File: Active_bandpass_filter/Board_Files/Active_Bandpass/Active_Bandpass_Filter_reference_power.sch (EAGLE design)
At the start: 35 parts, among them IC2 AD8031R, IC3 7805TV, IC5 AD8542R

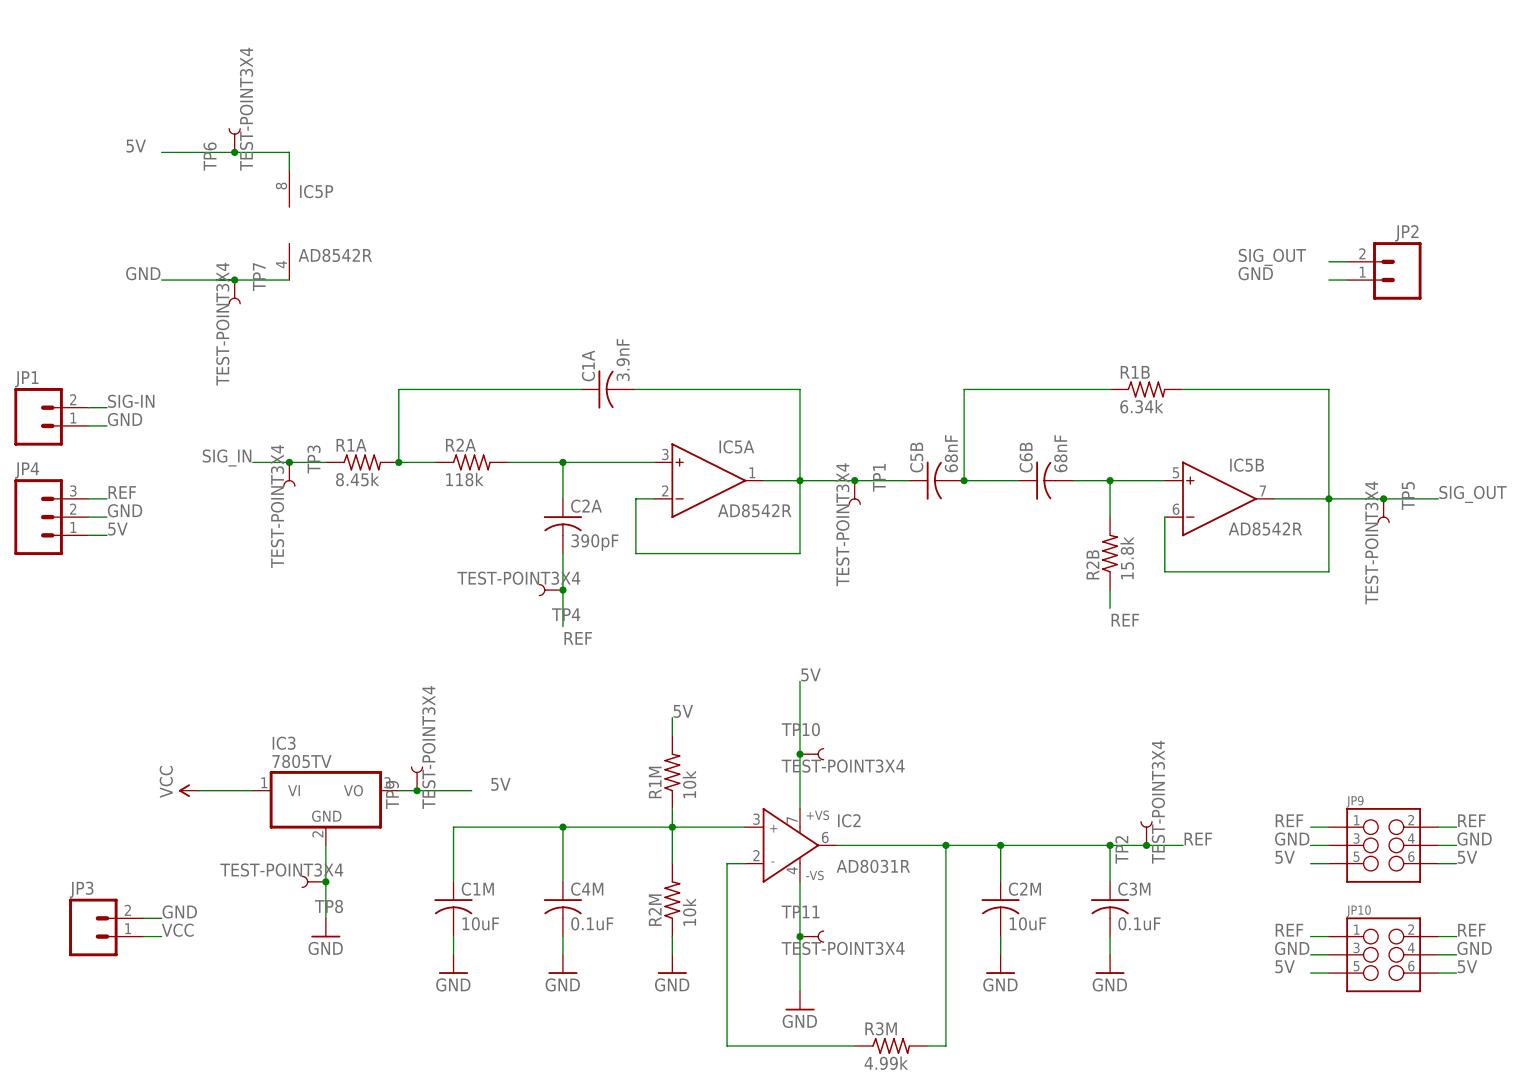
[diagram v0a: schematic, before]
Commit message: split into 2 boards
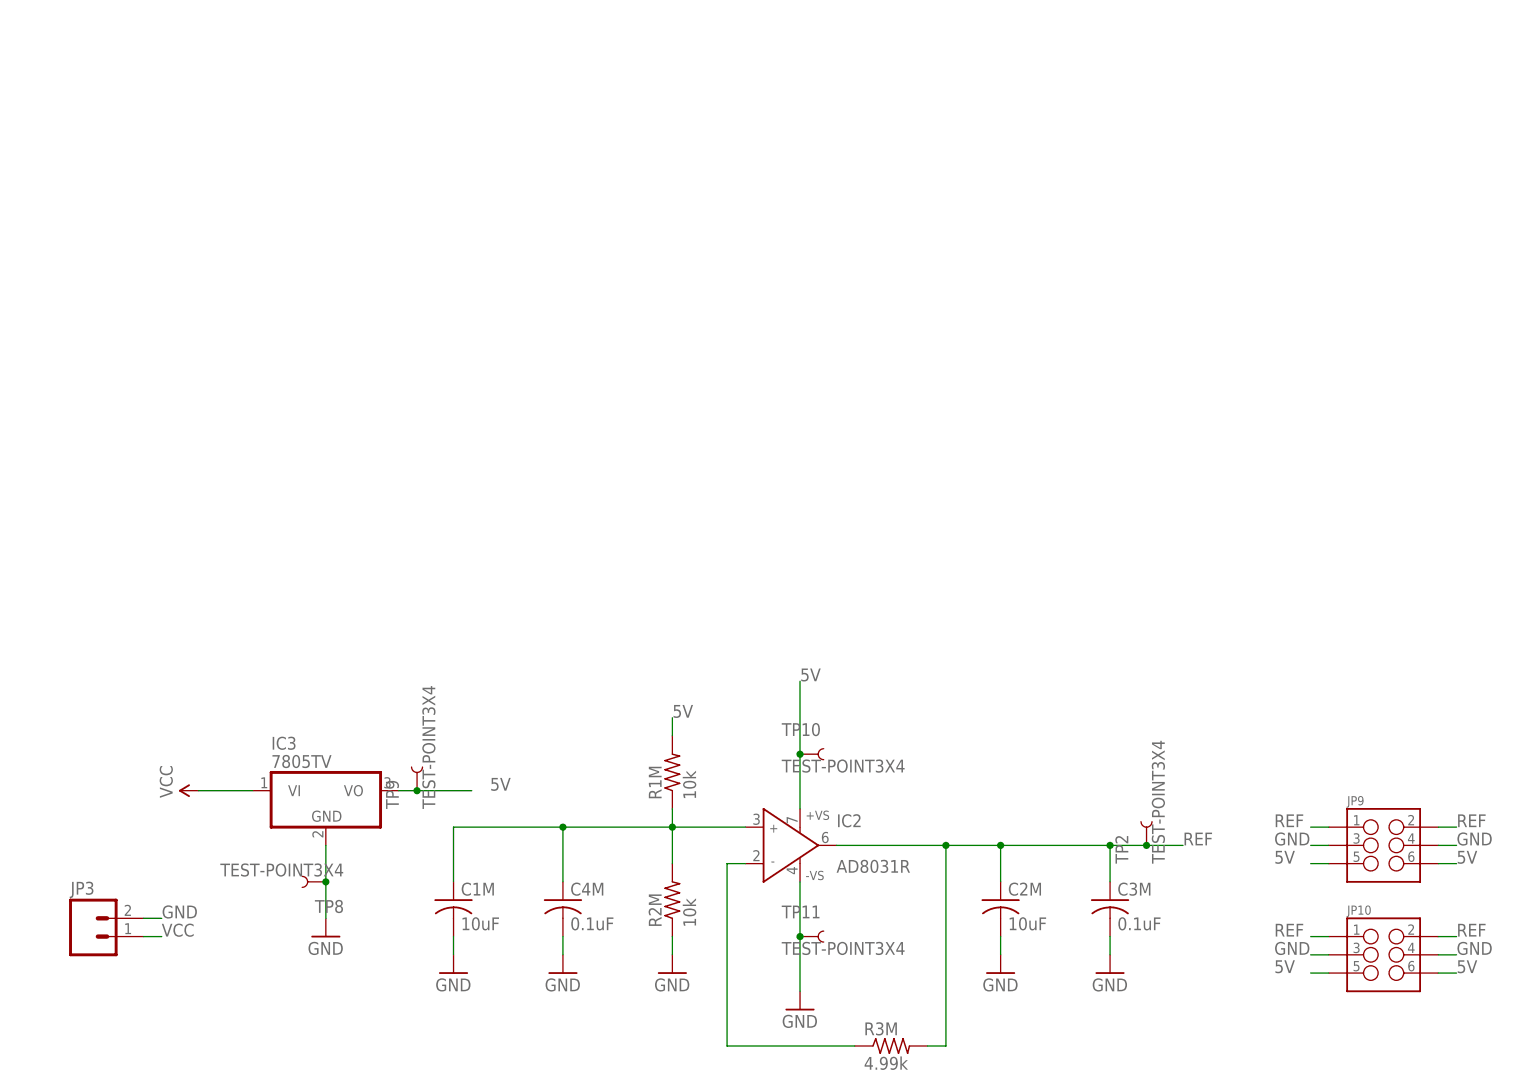
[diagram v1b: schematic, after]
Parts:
- removed C1A: 3.9nF, resistor:C-USC1206
- removed C2A: 390pF, resistor:C-USC1206
- removed C5B, C6B: 68nF, resistor:C-USC1206
- removed IC5: AD8542R, analog-devices:AD8542R
- removed JP1, JP2: (no value), SparkFun-Connectors:M02LOCK_LONGPADS
- removed JP4: (no value), SparkFun-Connectors:M03LOCK_LONGPADS
- removed R1A: 8.45k, resistor:R-US_R1206
- removed R1B: 6.34k, resistor:R-US_R1206
- removed R2A: 118k, resistor:R-US_R1206
- removed R2B: 15.8k, resistor:R-US_R1206
- removed TP1, TP3, TP4, TP5, TP6, TP7: TEST-POINT3X4, SparkFun-Passives:TEST-POINT3X4
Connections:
- removed net N$1: C1A.1, R1A.2, R2A.1
- removed net N$2: C2A.1, IC5A.IN+, R2A.2
- removed net N$3: C1A.2, C5B.1, IC5A.IN-, IC5A.OUT, TP1.1
- removed net N$4: C5B.2, C6B.1, R1B.1
- removed net N$5: C6B.2, IC5B.IN+, R2B.2
- removed net SIG-IN: JP1.2
- removed net SIG_IN: R1A.1, TP3.1
- removed net SIG_OUT: IC5B.IN-, IC5B.OUT, JP2.2, R1B.2, TP5.1
- net 5V: no longer IC5P.V+, JP4.1, TP6.1
- net GND: no longer IC5P.V-, JP1.1, JP2.1, JP4.2, TP7.1
- net REF: no longer C2A.2, JP4.3, R2B.1, TP4.1
